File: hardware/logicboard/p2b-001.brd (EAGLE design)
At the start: 91 x 90 mm, 51 parts, among them IC1 74LS06N, IC2 4066N, J1 MKR, J2 GPIO, J3 Vcc, J4 RLY, J5 SPI, J7 DIN5, J8 DIN5, J9 DIN5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

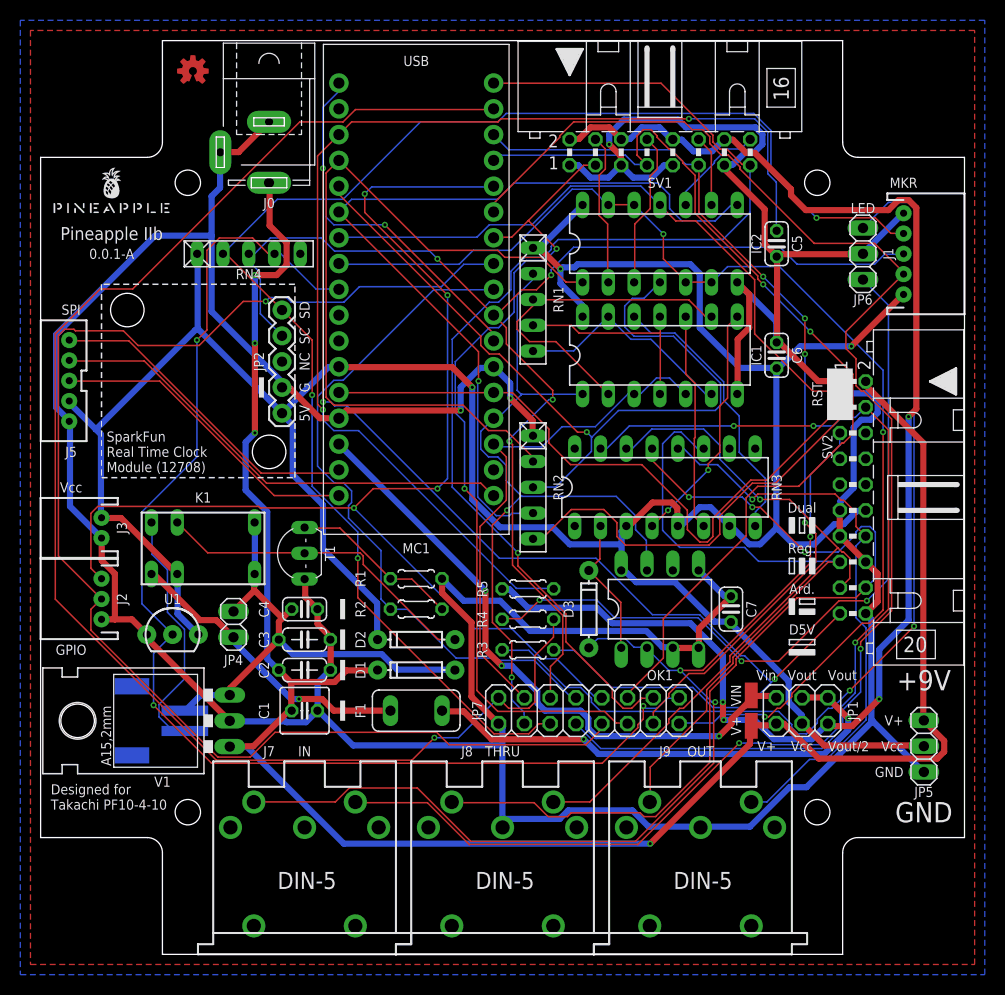
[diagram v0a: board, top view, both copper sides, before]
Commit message: Renumbered parts.
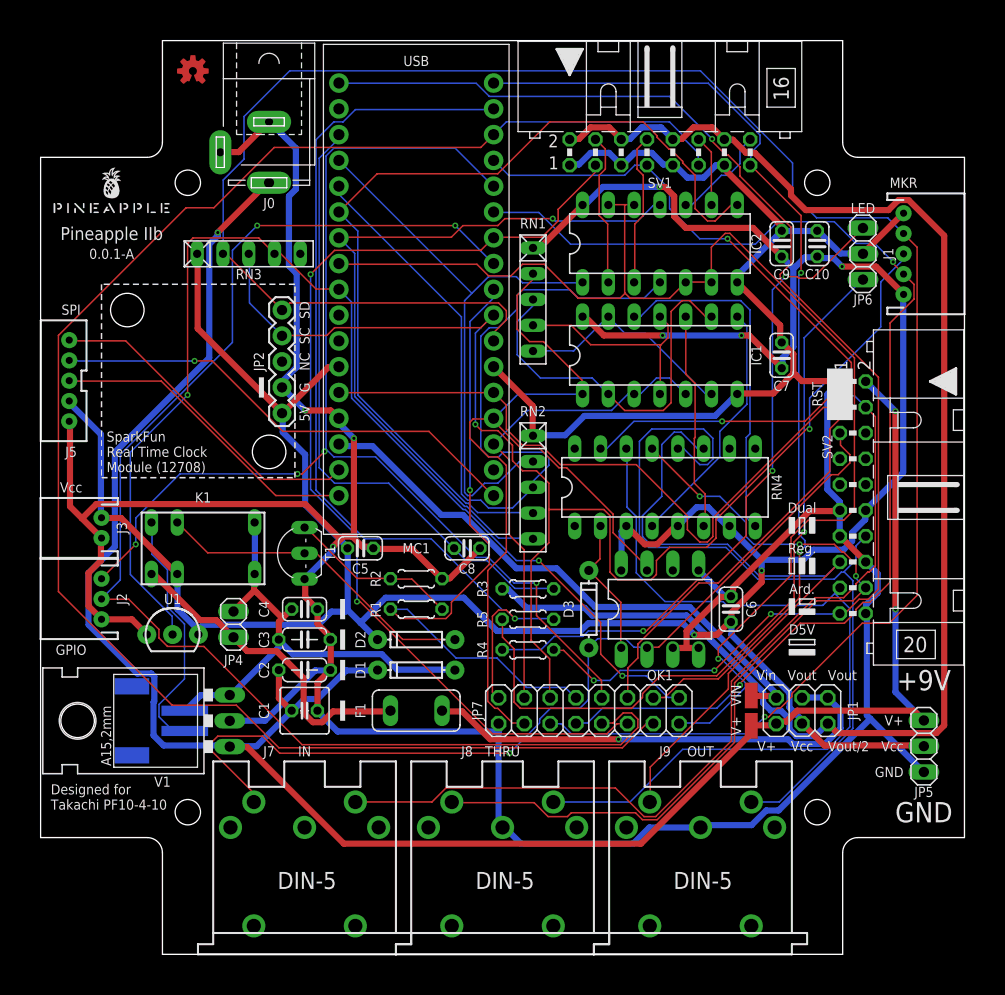
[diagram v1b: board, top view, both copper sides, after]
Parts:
- added C10: 100n, resistor:C025-024X044
- added C8: 100n, rcl:C025-024X044
- added C9: 10n, resistor:C025-024X044
- C5: value 100n -> 10n; device rcl:C025-024X044 -> resistor:C025-024X044
- R1: value 47k -> 1k
- R2: value 1k -> 47k
- RN3: value 220 -> 4.7k; device resistor-dil:DIL16 -> resistor-net:RN-5
- RN4: value 4.7k -> 220; device resistor-net:RN-5 -> resistor-dil:DIL16
- moved C5 50.8 mm to (31.5, 40.0), turned to 0 degrees
- moved RN3 47.0 mm to (20.5, 69.0)
- moved RN4 47.0 mm to (61.5, 46.0)
- moved C7 25.5 mm to (73.0, 59.0)
- moved C6 25.4 mm to (68.0, 34.0)
- moved R3 6.00 mm to (48.0, 36.0), turned to 180 degrees
- moved R1 3.00 mm to (37.0, 34.0)
- moved R2 3.00 mm to (37.0, 37.0)
- moved R4 3.00 mm to (48.0, 30.0)
- moved R5 3.00 mm to (48.0, 33.0), turned to 0 degrees
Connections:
- net AREF: now also C8.1, R3.1; no longer C5.1, R5.1
- net GND: now also C10.2, C8.2, C9.2, R2.1; no longer R1.1
- net LED0: now also R4.2; no longer R3.2
- net LED0A: now also R4.1; no longer R3.1
- net LED1: now also R5.2; no longer R4.2
- net LED1A: now also R5.1; no longer R4.1
- net MIDIINSND: now also RN4.2; no longer RN3.2
- net MISND: now also RN4.15; no longer RN3.15
- net MO2RTN: now also RN4.9; no longer RN3.9
- net MO2RTNRAW: now also RN4.8; no longer RN3.8
- net MO2SND: now also RN4.10; no longer RN3.10
- net MORTN: now also RN4.11; no longer RN3.11
- net MORTNRAW: now also RN4.6; no longer RN3.6
- net MOSND: now also RN4.12; no longer RN3.12
- net MTRTN: now also RN4.13; no longer RN3.13
- net MTRTNRAW: now also RN4.4; no longer RN3.4
- net MTSND: now also RN4.14; no longer RN3.14
- net RLY: now also R1.2; no longer R2.2
- net RLYDRV: now also R1.1, R2.2; no longer R1.2, R2.1
- net SCL: now also RN3.3; no longer RN4.3
- net SDA: now also RN3.2; no longer RN4.2
- net THS: now also RN3.4; no longer RN4.4
- net VCC: now also C10.1, C5.1, C9.1, RN3.1, RN4.3, RN4.5, RN4.7; no longer RN3.3, RN3.5, RN3.7, RN4.1
- net VCC/2: now also R3.2; no longer R5.2
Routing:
- net DTCT3: track 88.8 -> 165.5 mm, vias 4 -> 0
- net LED1: track 144.5 -> 93.1 mm
- net AREF: track 112.3 -> 61.7 mm, vias 2 -> 0
- net SDA: track 168.3 -> 202.5 mm, vias 4 -> 1
- net ANLG4: track 106.4 -> 72.8 mm, vias 0 -> 1
- net LED0A: track 96.5 -> 65.5 mm, vias 2 -> 3
- net GND: track 431.1 -> 402.0 mm
- net MOSND: track 56.9 -> 79.4 mm, vias 1 -> 0
- net DTCT4: track 116.2 -> 95.5 mm, vias 1 -> 2
- net VCC: track 288.6 -> 307.6 mm, vias 3 -> 6
- net ANLG1: track 76.1 -> 58.6 mm
- net D7: track 130.7 -> 113.6 mm, vias 1 -> 2
- net DTCT1: track 83.3 -> 100.2 mm
- net V+: track 195.7 -> 209.9 mm, vias 4 -> 3
- net MIRTN: track 104.0 -> 90.6 mm, vias 3 -> 1
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- removed copper zone on layer 1, net GND
- removed copper zone on layer 16, net GND

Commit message: Clean up.
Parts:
- C10: device resistor:C025-024X044 -> rcl:C025-024X044
- C8: value 100n -> 10n; device rcl:C025-024X044 -> resistor:C025-024X044
- C9: value 10n -> 100n
- moved C10 45.7 mm to (42.0, 40.0), turned to 0 degrees
- moved C8 43.1 mm to (73.0, 70.0), turned to 90 degrees
- moved C9 3.50 mm to (76.5, 70.0)
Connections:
- net AREF: now also C10.1; no longer C8.1
- net VCC: now also C8.1; no longer C10.1
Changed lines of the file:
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@@
 <grid distance="0.5" unitdist="mm" unit="mm" style="lines" multiple="2" display="yes" altdistance="50" altunitdist="mil" altunit="mil"/>
 <layers>
-<layer number="1" name="Top" color="4" fill="1" visible="no" active="yes"/>
-<layer number="16" name="Bottom" color="1" fill="1" visible="no" active="yes"/>
+<layer number="1" name="Top" color="4" fill="1" visible="yes" active="yes"/>
+<layer number="16" name="Bottom" color="1" fill="1" visible="yes" active="yes"/>
 <layer number="17" name="Pads" color="2" fill="1" visible="yes" active="yes"/>
 <layer number="18" name="Vias" color="2" fill="1" visible="yes" active="yes"/>
@@
 <attribute name="VALUE" x="50.1336" y="38.3114" size="0.9906" layer="27" ratio="10" rot="R180"/>
 </element>
-<element name="C8" library="rcl" library_urn="urn:adsk.eagle:library:334" package="C025-024X044" package3d_urn="urn:adsk.eagle:package:23630/1" value="100n" x="42" y="40" smashed="yes">
+<element name="C10" library="rcl" library_urn="urn:adsk.eagle:library:334" package="C025-024X044" package3d_urn="urn:adsk.eagle:package:23630/1" value="100n" x="42" y="40" smashed="yes">
 <attribute name="NAME" x="42" y="38" size="1" layer="25" ratio="10" rot="R180" align="center"/>
 <attribute name="POPULARITY" value="56" x="42" y="40" size="1.778" layer="27" display="off"/>
@@
 <attribute name="VALUE" x="29.722" y="37.333" size="1.27" layer="27" ratio="10"/>
 </element>
-<element name="C9" library="resistor" library_urn="urn:adsk.eagle:library:348" package="C025-024X044" package3d_urn="urn:adsk.eagle:package:23630/1" value="10n" x="73" y="70" smashed="yes" rot="R90">
+<element name="C8" library="resistor" library_urn="urn:adsk.eagle:library:348" package="C025-024X044" package3d_urn="urn:adsk.eagle:package:23630/1" value="10n" x="73" y="70" smashed="yes" rot="R90">
 <attribute name="NAME" x="73" y="67" size="1" layer="25" ratio="10" align="center"/>
 <attribute name="VALUE" x="75.667" y="68.222" size="1.27" layer="27" ratio="10" rot="R90"/>
 </element>
-<element name="C10" library="resistor" library_urn="urn:adsk.eagle:library:348" package="C025-024X044" package3d_urn="urn:adsk.eagle:package:23630/1" value="100n" x="76.5" y="70" smashed="yes" rot="R90">
+<element name="C9" library="resistor" library_urn="urn:adsk.eagle:library:348" package="C025-024X044" package3d_urn="urn:adsk.eagle:package:23630/1" value="100n" x="76.5" y="70" smashed="yes" rot="R90">
 <attribute name="NAME" x="76.5" y="67" size="1" layer="25" ratio="10" align="center"/>
 <attribute name="VALUE" x="79.167" y="68.222" size="1.27" layer="27" ratio="10" rot="R90"/>
@@
 <contactref element="C6" pad="2"/>
 <contactref element="C7" pad="2"/>
-<contactref element="C8" pad="2"/>
+<contactref element="C10" pad="2"/>
 <contactref element="MC1" pad="P$21"/>
 <contactref element="MC1" pad="P$12"/>
@@
 <contactref element="SV2" pad="16"/>
 <contactref element="JP6" pad="2"/>
-<contactref element="JP5" pad="1"/>
 <contactref element="J0" pad="2"/>
 <contactref element="J0" pad="1"/>
@@
 <contactref element="JP7" pad="1"/>
 <contactref element="C5" pad="2"/>
+<contactref element="C8" pad="2"/>
 <contactref element="C9" pad="2"/>
-<contactref element="C10" pad="2"/>
+<contactref element="JP5" pad="1"/>
 <wire x1="64.77" y1="30.1752" x2="63.627" y2="30.1752" width="0.6096" layer="1"/>
 <wire x1="63.627" y1="30.1752" x2="62.3316" y2="30.1752" width="0.6096" layer="1"/>
@@
 <contactref element="OK1" pad="8"/>
 <contactref element="SV2" pad="12"/>
+<contactref element="C5" pad="1"/>
+<contactref element="C8" pad="1"/>
+<contactref element="C9" pad="1"/>
 <contactref element="JP5" pad="2"/>
-<contactref element="C5" pad="1"/>
-<contactref element="C9" pad="1"/>
-<contactref element="C10" pad="1"/>
 <wire x1="15.4686" y1="61.6458" x2="15.4686" y2="68.961" width="0.6096" layer="1"/>
 <wire x1="23.7744" y1="53.34" x2="15.4686" y2="61.6458" width="0.6096" layer="1"/>
@@
 <signal name="AREF">
 <contactref element="R3" pad="1"/>
-<contactref element="C8" pad="1"/>
+<contactref element="C10" pad="1"/>
 <contactref element="MC1" pad="P$32"/>
 <wire x1="46.7106" y1="36.0426" x2="50.5206" y2="36.0426" width="0.1524" layer="16"/>
@@
 <contactref element="SV2" pad="2"/>
 <contactref element="V+" pad="1"/>
+<contactref element="J0" pad="3"/>
 <contactref element="JP5" pad="3"/>
-<contactref element="J0" pad="3"/>
 <wire x1="72.2376" y1="22.5552" x2="70.0278" y2="22.5552" width="0.6096" layer="1"/>
 <wire x1="72.39" y1="22.7076" x2="72.2376" y2="22.5552" width="0.6096" layer="1"/>

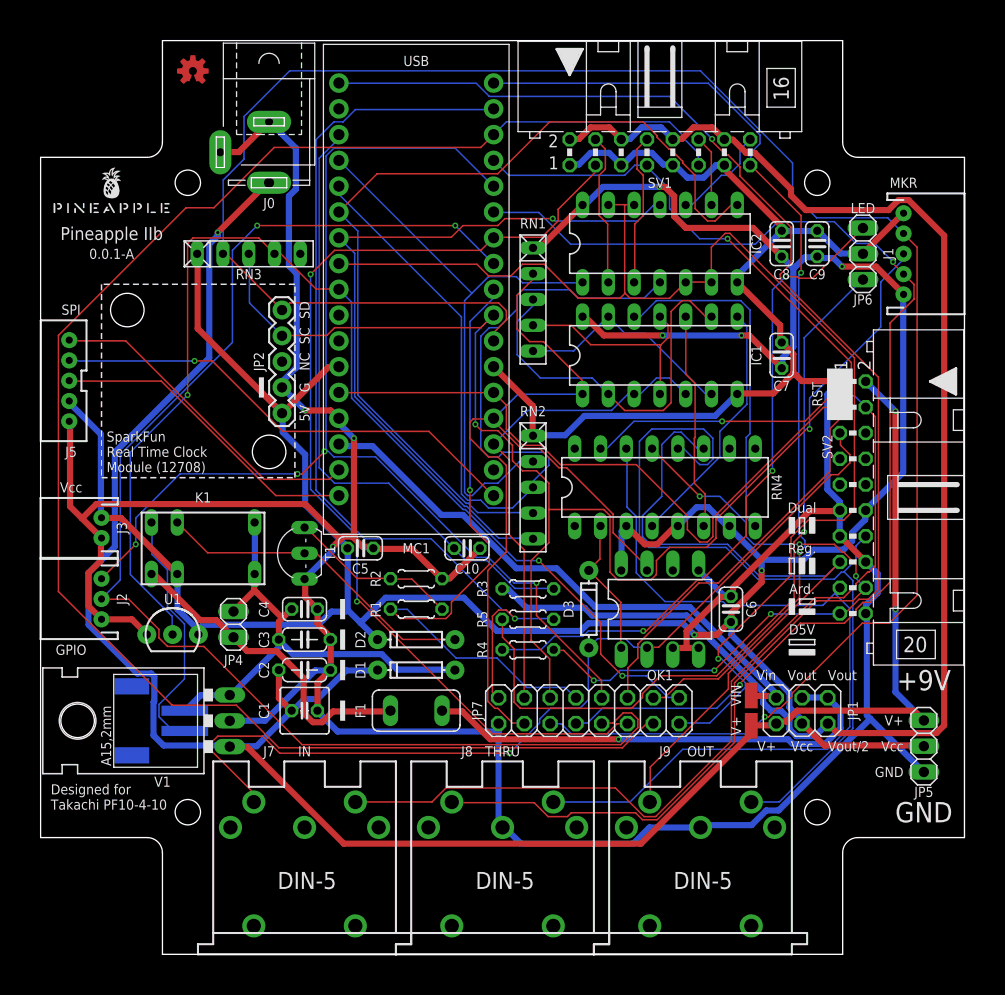
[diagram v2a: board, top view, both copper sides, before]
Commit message: New back port, broader power pattern.
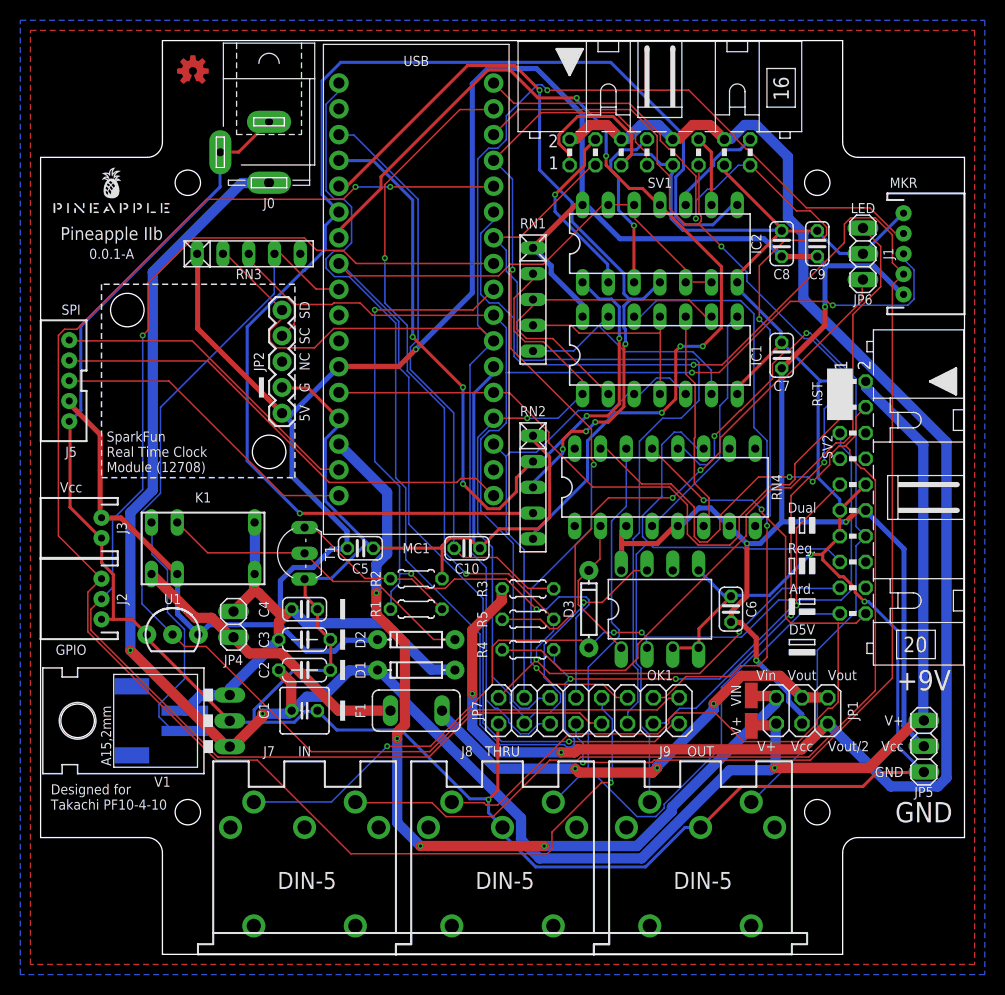
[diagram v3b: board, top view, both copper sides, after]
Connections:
- net GND: now also SV2.10; no longer SV2.16, SV2.20
- net LED0: now also SV2.9; no longer SV2.19
- net LED1: now also SV2.17
- net MRX+: now also SV2.6; no longer SV2.7
- net MRXDTCT: now also SV2.7; no longer SV2.6
- net MTRTN: now also SV2.20; no longer SV2.18
- net MTSND: now also SV2.19; no longer SV2.17
- net MTX+: now also SV2.16; no longer SV2.9
- net MTX-: now also SV2.18; no longer SV2.10
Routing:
- net DTCT3: track 165.5 -> 101.1 mm, vias 0 -> 3
- net SDA: track 202.5 -> 151.7 mm
- net GPIO2: track 116.3 -> 153.8 mm, vias 4 -> 3
- net ANLG3: track 90.6 -> 127.0 mm, vias 0 -> 1
- net VIN: track 56.3 -> 88.6 mm, vias 0 -> 4
- net D7: track 113.6 -> 144.6 mm
- net GND: track 402.0 -> 428.7 mm
- net ANLG4: track 72.8 -> 94.3 mm, vias 1 -> 5
- net LED1A: track 75.4 -> 56.8 mm, vias 1 -> 2
- net LED1: track 93.1 -> 110.1 mm, vias 1 -> 4
- net DTCT1: track 100.2 -> 83.7 mm, vias 2 -> 0
- net VCC/2: track 145.2 -> 161.3 mm, vias 0 -> 2
- net ANLG1: track 58.6 -> 74.6 mm, vias 0 -> 5
- net VCC: track 307.6 -> 321.2 mm, vias 6 -> 5
- net DTCT4: track 95.5 -> 107.6 mm, vias 2 -> 3
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- added copper zone on layer 1, net GND
- added copper zone on layer 16, net GND

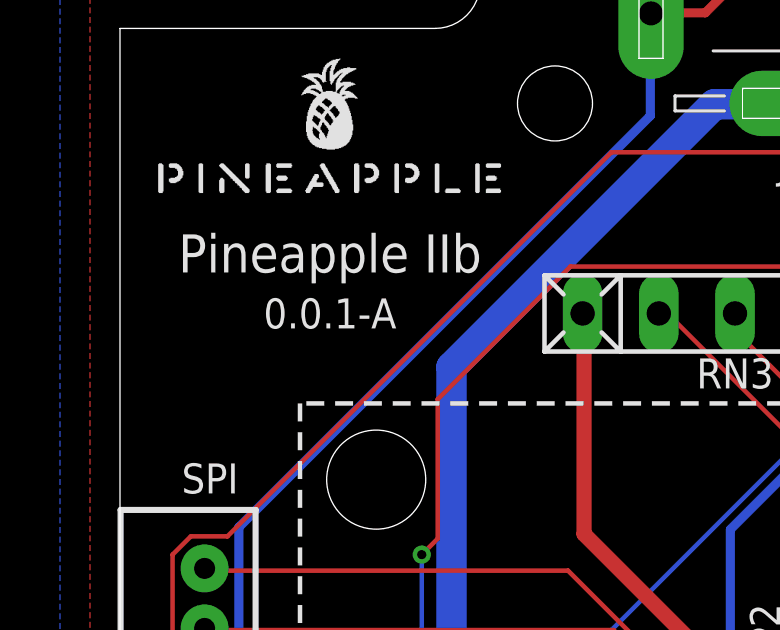
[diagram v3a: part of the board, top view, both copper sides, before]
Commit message: LED0->LED1, LED1->LED2.
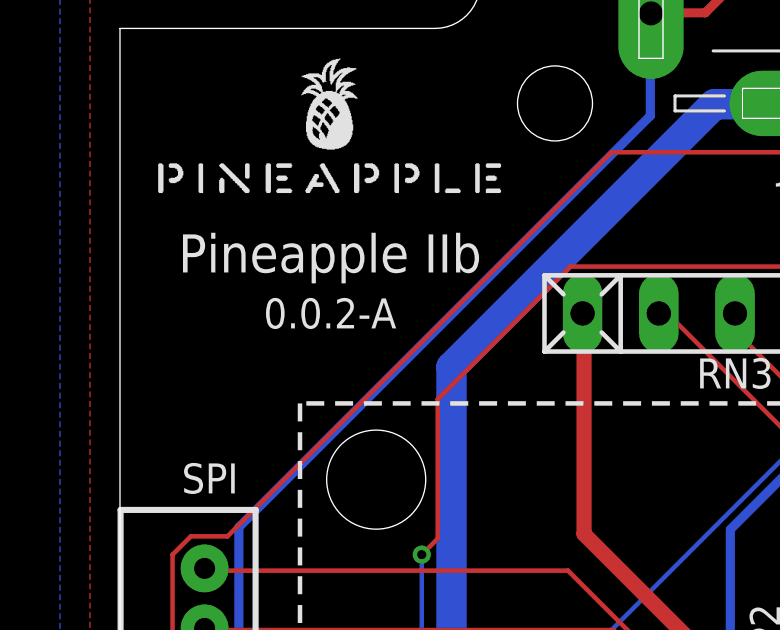
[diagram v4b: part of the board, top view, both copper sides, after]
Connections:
- removed net LED0: MC1.P$34, R4.2, SV2.9
- new net LED2: JP7.2, MC1.P$2, R5.2, SV2.17
- net LED1: now also MC1.P$34, R4.2, SV2.9; no longer JP7.2, MC1.P$2, R5.2, SV2.17
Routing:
- net LED0: track 133.9 -> 0.00 mm, vias 3 -> 0
- net LED2: track 0.00 -> 110.1 mm, vias 0 -> 4
- net LED1: track 110.1 -> 133.9 mm, vias 4 -> 3
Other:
- board text added: "0.0.2-A"
- board text removed: "0.0.1-A"
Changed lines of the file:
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@@
 <wire x1="25.05" y1="66" x2="6" y2="66" width="0.15" layer="21" style="dashdot"/>
 <wire x1="6" y1="66" x2="6" y2="46.95" width="0.15" layer="21" style="dashdot"/>
-<text x="7" y="69" size="1" layer="25" align="center">0.0.1-A</text>
+<text x="7" y="69" size="1" layer="25" align="center">0.0.2-A</text>
 <text x="26" y="63.46" size="1" layer="25" rot="R90" align="center">SD</text>
 <text x="26" y="60.92" size="1" layer="25" rot="R90" align="center">SC</text>
@@
 <via x="70.7898" y="62.5602" extent="1-16" drill="0.3048"/>
 </signal>
-<signal name="LED0">
+<signal name="LED1">
 <contactref element="MC1" pad="P$34"/>
 <contactref element="R4" pad="2"/>
@@
 <contactref element="MC1" pad="P$33"/>
 </signal>
-<signal name="LED1">
+<signal name="LED2">
 <contactref element="MC1" pad="P$2"/>
 <contactref element="R5" pad="2"/>
